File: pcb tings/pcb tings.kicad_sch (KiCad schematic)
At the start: 24 parts

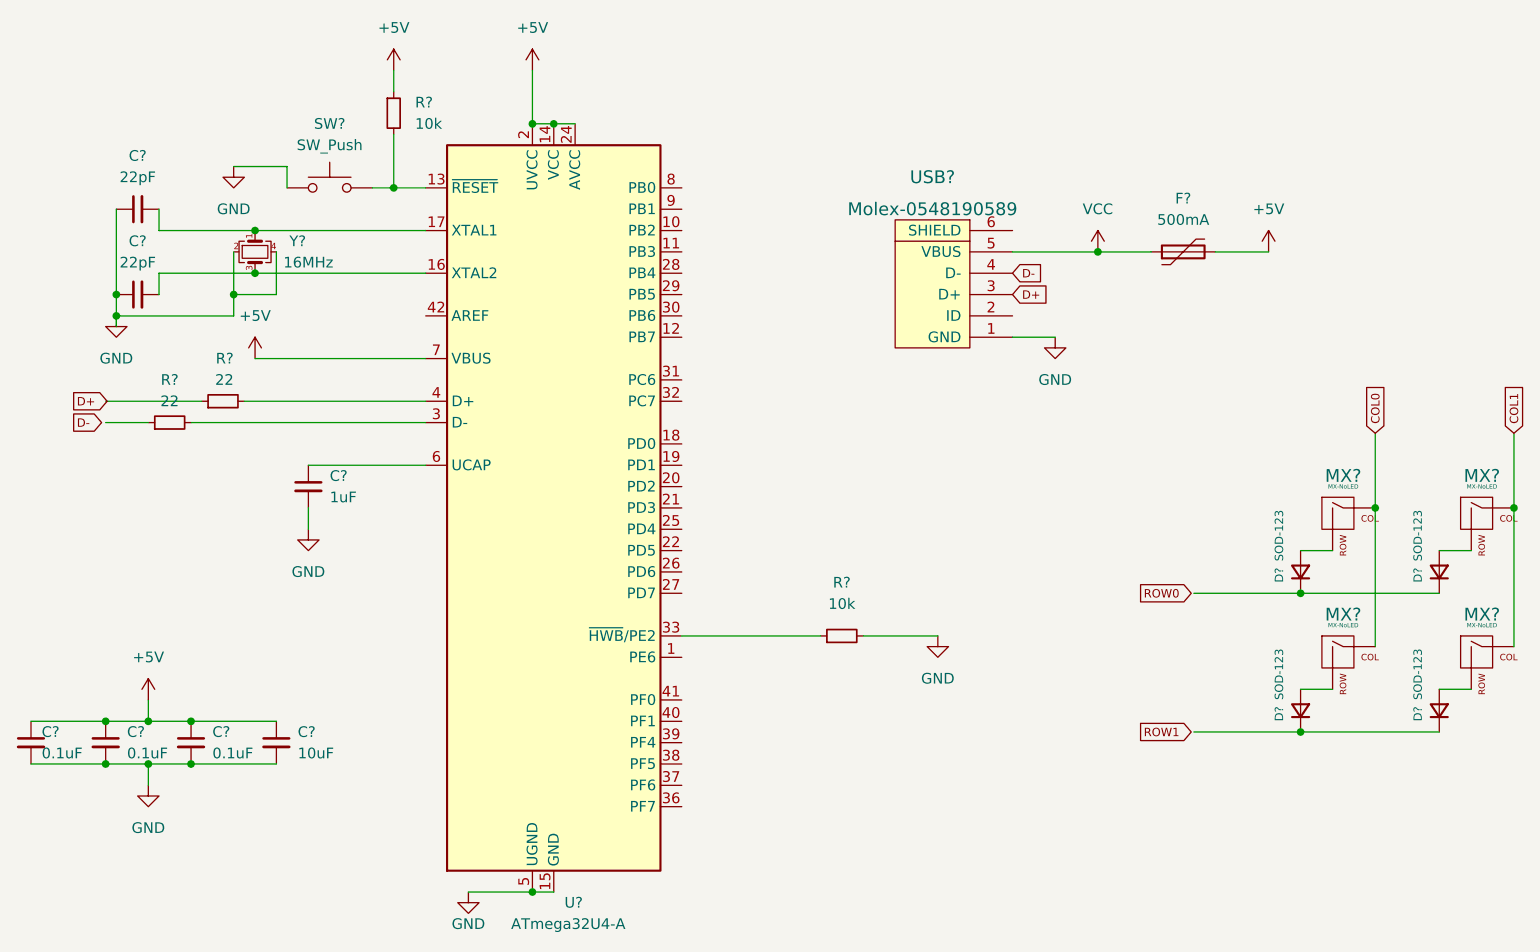
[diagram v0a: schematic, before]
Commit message: Added the footprints to the schema (the software needs to know the shape of the components) Here are a few links. Dont connect the shield on the USB to anything. https://forum.arduino.cc/t/where-do-you-connect-shield-pins-on-usb-port/439330/11
and we should be go to go to create the PCB and start the layout itself.
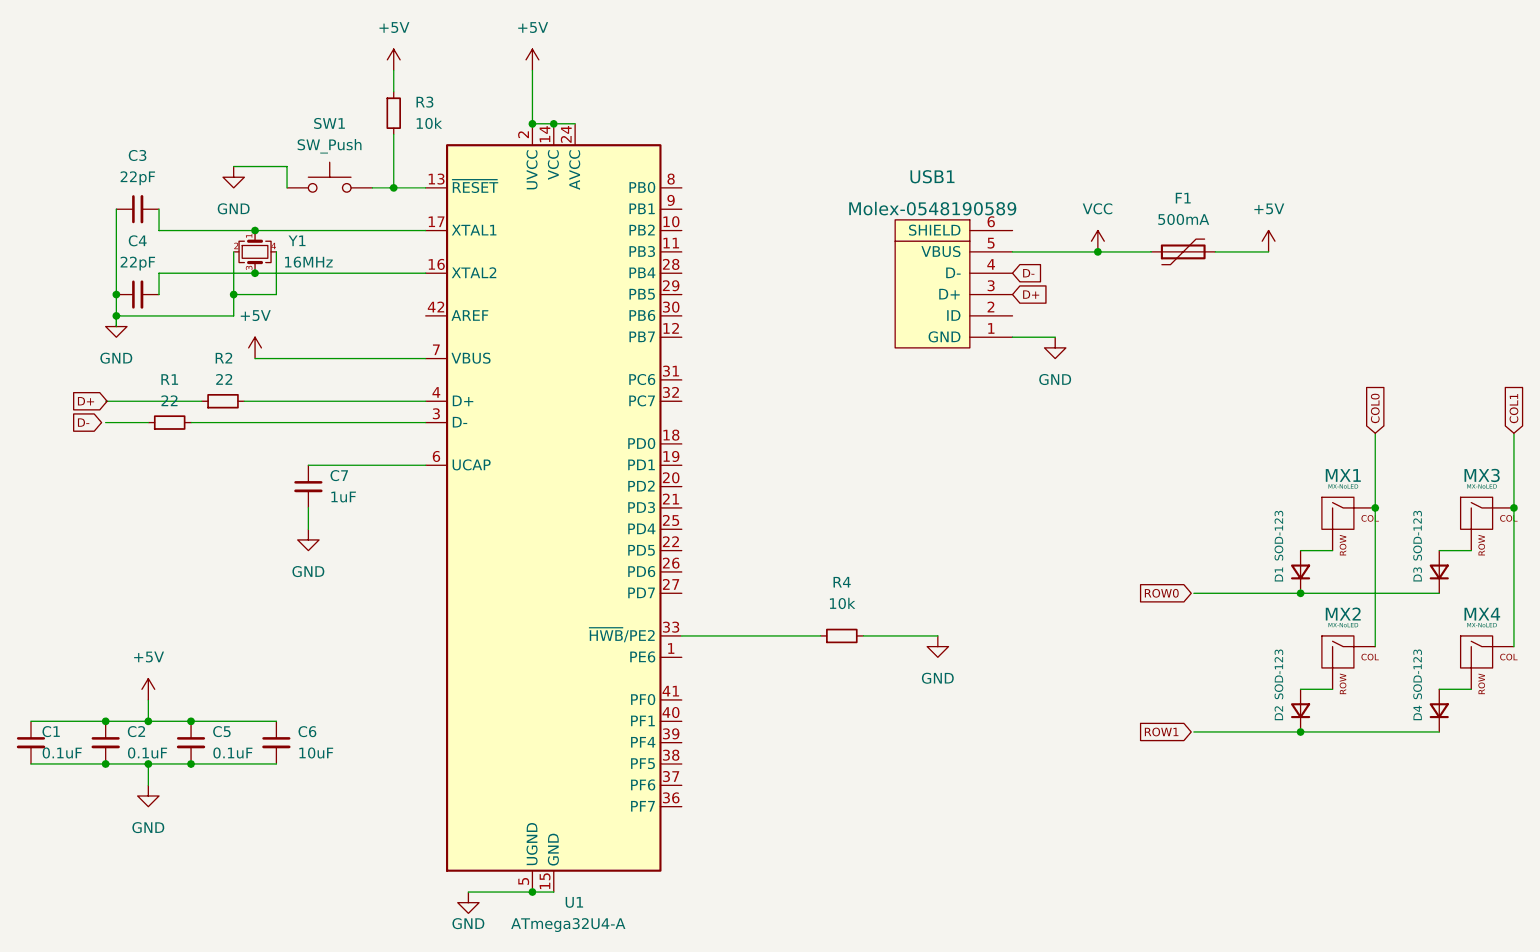
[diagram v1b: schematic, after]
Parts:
- C1, C2, C3, C4, C5, C6, C7: renamed from C?; footprint (none) -> Capacitor_SMD:C_0805_2012Metric
- D1, D2, D3, D4: renamed from D?; footprint (none) -> Diode_SMD:D_SOD-123
- F1: renamed from F?; footprint (none) -> Fuse:Fuse_1206_3216Metric
- MX1, MX2, MX3, MX4: renamed from MX?; footprint (none) -> MX_Alps_Hybrid:MX-1U-NoLED
- R1, R2, R3, R4: renamed from R?; footprint (none) -> Resistor_SMD:R_0805_2012Metric
- SW1: renamed from SW?; footprint (none) -> random-keyboard-parts:SKQG-1155865
- USB1: renamed from USB?; footprint (none) -> random-keyboard-parts:Molex-0548190589
- Y1: renamed from Y?; footprint (none) -> Crystal:Crystal_SMD_3225-4Pin_3.2x2.5mm
- gave numbers to parts that had none: 1
